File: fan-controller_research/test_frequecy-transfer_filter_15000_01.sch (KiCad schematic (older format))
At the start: 25 parts, among them U401 TL071

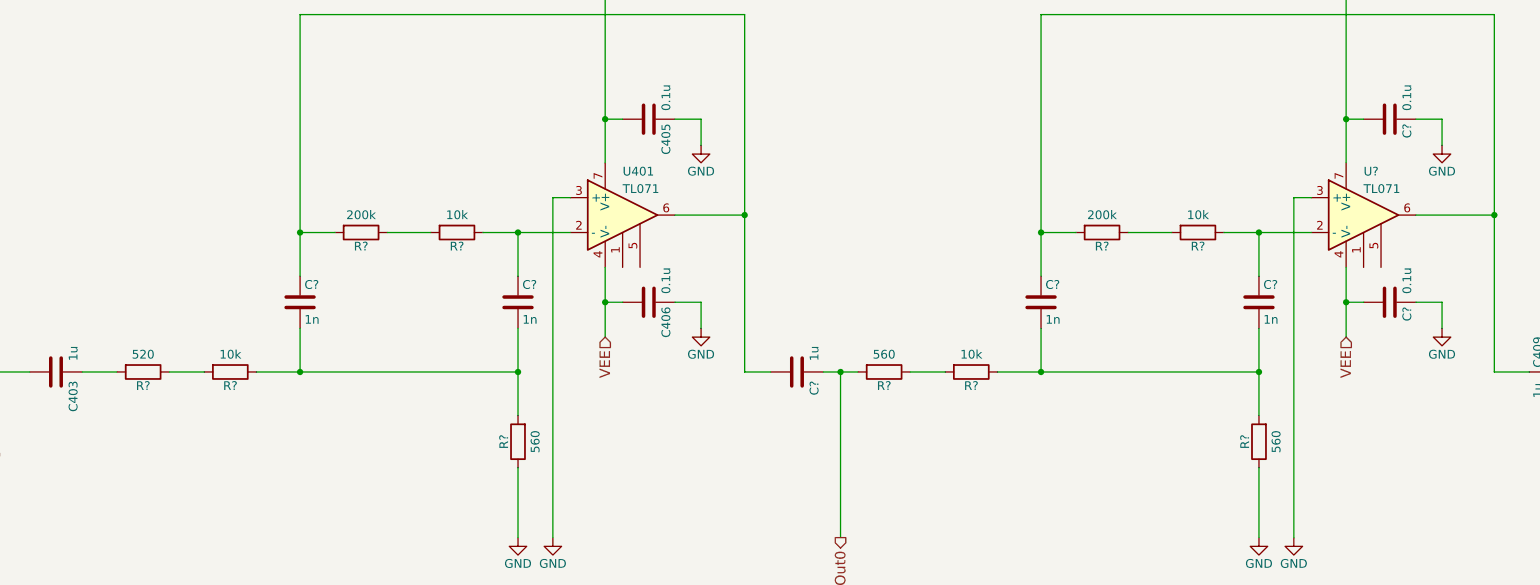
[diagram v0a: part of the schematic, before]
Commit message: Annotating schematics: 15000 Hz research filter
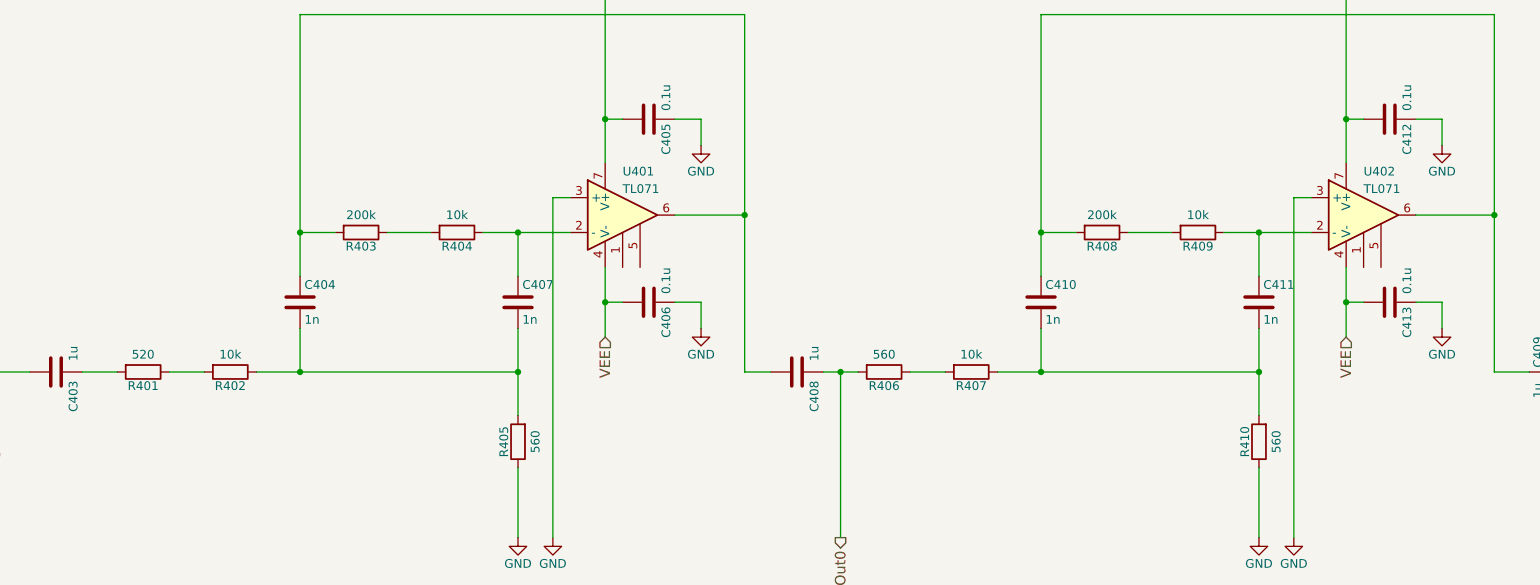
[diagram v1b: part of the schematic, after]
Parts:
- gave numbers to parts that had none: 18
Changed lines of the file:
@@
 $EndComp
 $Comp
-L AC #PWR013
+L AC #PWR404
 U 1 1 59072200
 P 3550 5100
-F 0 "#PWR013" H 3550 5000 50  0001 C CNN
+F 0 "#PWR404" H 3550 5000 50  0001 C CNN
 F 1 "AC" V 3300 5250 50  0000 C CNN
 F 2 "" H 3550 5100 50  0001 C CNN
@@
 $EndComp
 $Comp
-L GND #PWR014
+L GND #PWR405
 U 1 1 59072206
 P 3550 5450
-F 0 "#PWR014" H 3550 5200 50  0001 C CNN
+F 0 "#PWR405" H 3550 5200 50  0001 C CNN
 F 1 "GND" H 3550 5300 50  0000 C CNN
 F 2 "" H 3550 5450 50  0001 C CNN
@@
 $EndComp
 $Comp
-L GND #PWR015
+L GND #PWR411
 U 1 1 5907220C
 P 11050 5450
-F 0 "#PWR015" H 11050 5200 50  0001 C CNN
+F 0 "#PWR411" H 11050 5200 50  0001 C CNN
 F 1 "GND" H 11050 5300 50  0000 C CNN
 F 2 "" H 11050 5450 50  0001 C CNN
@@
 Spectrum analyzer output, 0 Hz ... 50 kHz.\n\nMarker is at 15 kHz.
 $Comp
-L +15V #PWR016
+L +15V #PWR401
 U 1 1 5907222C
 P 1000 850
-F 0 "#PWR016" H 1000 700 50  0001 C CNN
+F 0 "#PWR401" H 1000 700 50  0001 C CNN
 F 1 "+15V" H 1000 990 50  0000 C CNN
 F 2 "" H 1000 850 50  0001 C CNN
@@
 $EndComp
 $Comp
-L -15V #PWR404
+L -15V #PWR402
 U 1 1 59072240
 P 1000 2100
-F 0 "#PWR404" H 1000 2200 50  0001 C CNN
+F 0 "#PWR402" H 1000 2200 50  0001 C CNN
 F 1 "-15V" H 1000 2250 50  0000 C CNN
 F 2 "" H 1000 2100 50  0001 C CNN
@@
 VEE
 $Comp
-L GND #PWR017
+L GND #PWR403
 U 1 1 59072248
 P 1500 1550
-F 0 "#PWR017" H 1500 1300 50  0001 C CNN
+F 0 "#PWR403" H 1500 1300 50  0001 C CNN
 F 1 "GND" H 1500 1400 50  0000 C CNN
 F 2 "" H 1500 1550 50  0001 C CNN
@@
 $EndComp
 $Comp
-L GND #PWR018
+L GND #PWR408
 U 1 1 5907226B
 P 7650 3200
-F 0 "#PWR018" H 7650 2950 50  0001 C CNN
+F 0 "#PWR408" H 7650 2950 50  0001 C CNN
 F 1 "GND" H 7650 3050 50  0000 C CNN
 F 2 "" H 7650 3200 50  0001 C CNN
@@
 $EndComp
 $Comp
-L GND #PWR019
+L GND #PWR409
 U 1 1 59072271
 P 7650 4250
-F 0 "#PWR019" H 7650 4000 50  0001 C CNN
+F 0 "#PWR409" H 7650 4000 50  0001 C CNN
 F 1 "GND" H 7650 4100 50  0000 C CNN
 F 2 "" H 7650 4250 50  0001 C CNN
@@
 Two times cascaded: \n15 kHz band pass, using a \nmodified Deliyannis filter\n(Texas Instruments, SLOA093)
 $Comp
-L R R?
+L R R401
 U 1 1 590DFFD6
 P 4450 4500
-F 0 "R?" V 4530 4500 50  0000 C CNN
+F 0 "R401" V 4530 4500 50  0000 C CNN
 F 1 "520" V 4350 4500 50  0000 C CNN
 F 2 "" V 4380 4500 50  0001 C CNN
@@
 $EndComp
 $Comp
-L R R?
+L R R402
 U 1 1 590E0205
 P 4950 4500
-F 0 "R?" V 5030 4500 50  0000 C CNN
+F 0 "R402" V 5030 4500 50  0000 C CNN
 F 1 "10k" V 4850 4500 50  0000 C CNN
 F 2 "" V 4880 4500 50  0001 C CNN
@@
 $EndComp
 $Comp
-L C C?
+L C C404
 U 1 1 590E0538
 P 5350 4100
-F 0 "C?" H 5375 4200 50  0000 L CNN
+F 0 "C404" H 5375 4200 50  0000 L CNN
 F 1 "1n" H 5375 4000 50  0000 L CNN
 F 2 "" H 5388 3950 50  0001 C CNN
@@
 $EndComp
 $Comp
-L C C?
+L C C407
 U 1 1 590E08E5
 P 6600 4100
-F 0 "C?" H 6625 4200 50  0000 L CNN
+F 0 "C407" H 6625 4200 50  0000 L CNN
 F 1 "1n" H 6625 4000 50  0000 L CNN
 F 2 "" H 6638 3950 50  0001 C CNN
@@
 $EndComp
 $Comp
-L R R?
+L R R403
 U 1 1 590E0977
 P 5700 3700
-F 0 "R?" V 5780 3700 50  0000 C CNN
+F 0 "R403" V 5780 3700 50  0000 C CNN
 F 1 "200k" V 5600 3700 50  0000 C CNN
 F 2 "" V 5630 3700 50  0001 C CNN
@@
 $EndComp
 $Comp
-L R R?
+L R R404
 U 1 1 590E0A08
 P 6250 3700
-F 0 "R?" V 6330 3700 50  0000 C CNN
+F 0 "R404" V 6330 3700 50  0000 C CNN
 F 1 "10k" V 6150 3700 50  0000 C CNN
 F 2 "" V 6180 3700 50  0001 C CNN
@@
 $EndComp
 $Comp
-L R R?
+L R R405
 U 1 1 590E1314
 P 6600 4900
-F 0 "R?" V 6680 4900 50  0000 C CNN
+F 0 "R405" V 6680 4900 50  0000 C CNN
 F 1 "560" V 6500 4900 50  0000 C CNN
 F 2 "" V 6530 4900 50  0001 C CNN
@@
 $EndComp
 $Comp
-L GND #PWR?
+L GND #PWR406
 U 1 1 590E1431
 P 6600 5450
-F 0 "#PWR?" H 6600 5200 50  0001 C CNN
+F 0 "#PWR406" H 6600 5200 50  0001 C CNN
 F 1 "GND" H 6600 5300 50  0000 C CNN
 F 2 "" H 6600 5450 50  0001 C CNN
@@
 $EndComp
 $Comp
-L TL071 U?
+L TL071 U402
 U 1 1 590E2308
 P 11450 3600
-F 0 "U?" H 11450 3850 50  0000 L CNN
+F 0 "U402" H 11450 3850 50  0000 L CNN
 F 1 "TL071" H 11450 3750 50  0000 L CNN
 F 2 "" H 11500 3650 50  0001 C CNN
@@
 $EndComp
 $Comp
-L C C?
+L C C408
 U 1 1 590E230E
 P 8200 4500
-F 0 "C?" H 8250 4600 50  0000 L CNN
+F 0 "C408" H 8250 4600 50  0000 L CNN
 F 1 "1u" H 8050 4600 50  0000 L CNN
 F 2 "" H 8238 4350 50  0001 C CNN
@@
 $EndComp
 $Comp
-L GND #PWR?
+L GND #PWR412
 U 1 1 590E2318
 P 11900 3200
-F 0 "#PWR?" H 11900 2950 50  0001 C CNN
+F 0 "#PWR412" H 11900 2950 50  0001 C CNN
 F 1 "GND" H 11900 3050 50  0000 C CNN
 F 2 "" H 11900 3200 50  0001 C CNN
@@
 $EndComp
 $Comp
-L GND #PWR?
+L GND #PWR413
 U 1 1 590E231E
 P 11900 4250
-F 0 "#PWR?" H 11900 4000 50  0001 C CNN
+F 0 "#PWR413" H 11900 4000 50  0001 C CNN
 F 1 "GND" H 11900 4100 50  0000 C CNN
 F 2 "" H 11900 4250 50  0001 C CNN
@@
 $EndComp
 $Comp
-L C C?
+L C C412
 U 1 1 590E2324
 P 11600 3050
-F 0 "C?" H 11625 3150 50  0000 L CNN
+F 0 "C412" H 11625 3150 50  0000 L CNN
 F 1 "0.1u" H 11400 3150 50  0000 L CNN
 F 2 "" H 11638 2900 50  0001 C CNN
@@
 $EndComp
 $Comp
-L C C?
+L C C413
 U 1 1 590E232A
 P 11600 4100
-F 0 "C?" H 11625 4200 50  0000 L CNN
+F 0 "C413" H 11625 4200 50  0000 L CNN
 F 1 "0.1u" H 11400 4200 50  0000 L CNN
 F 2 "" H 11638 3950 50  0001 C CNN
@@
 VEE
 $Comp
-L R R?
+L R R406
 U 1 1 590E233A
 P 8700 4500
-F 0 "R?" V 8780 4500 50  0000 C CNN
+F 0 "R406" V 8780 4500 50  0000 C CNN
 F 1 "560" V 8600 4500 50  0000 C CNN
 F 2 "" V 8630 4500 50  0001 C CNN
@@
 $EndComp
 $Comp
-L R R?
+L R R407
 U 1 1 590E2340
 P 9200 4500
-F 0 "R?" V 9280 4500 50  0000 C CNN
+F 0 "R407" V 9280 4500 50  0000 C CNN
 F 1 "10k" V 9100 4500 50  0000 C CNN
 F 2 "" V 9130 4500 50  0001 C CNN
@@
 $EndComp
 $Comp
-L C C?
+L C C410
 U 1 1 590E2346
 P 9600 4100
-F 0 "C?" H 9625 4200 50  0000 L CNN
+F 0 "C410" H 9625 4200 50  0000 L CNN
 F 1 "1n" H 9625 4000 50  0000 L CNN
 F 2 "" H 9638 3950 50  0001 C CNN
@@
 $EndComp
 $Comp
-L C C?
+L C C411
 U 1 1 590E234C
 P 10850 4100
-F 0 "C?" H 10875 4200 50  0000 L CNN
+F 0 "C411" H 10875 4200 50  0000 L CNN
 F 1 "1n" H 10875 4000 50  0000 L CNN
 F 2 "" H 10888 3950 50  0001 C CNN
@@
 $EndComp
 $Comp
-L R R?
+L R R408
 U 1 1 590E2352
 P 9950 3700
-F 0 "R?" V 10030 3700 50  0000 C CNN
+F 0 "R408" V 10030 3700 50  0000 C CNN
 F 1 "200k" V 9850 3700 50  0000 C CNN
 F 2 "" V 9880 3700 50  0001 C CNN
@@
 $EndComp
 $Comp
-L R R?
+L R R409
 U 1 1 590E2358
 P 10500 3700
-F 0 "R?" V 10580 3700 50  0000 C CNN
+F 0 "R409" V 10580 3700 50  0000 C CNN
 F 1 "10k" V 10400 3700 50  0000 C CNN
 F 2 "" V 10430 3700 50  0001 C CNN
@@
 $EndComp
 $Comp
-L R R?
+L R R410
 U 1 1 590E236B
 P 10850 4900
-F 0 "R?" V 10930 4900 50  0000 C CNN
+F 0 "R410" V 10930 4900 50  0000 C CNN
 F 1 "560" V 10750 4900 50  0000 C CNN
 F 2 "" V 10780 4900 50  0001 C CNN
@@
 $EndComp
 $Comp
-L GND #PWR?
+L GND #PWR410
 U 1 1 590E2372
 P 10850 5450
-F 0 "#PWR?" H 10850 5200 50  0001 C CNN
+F 0 "#PWR410" H 10850 5200 50  0001 C CNN
 F 1 "GND" H 10850 5300 50  0000 C CNN
 F 2 "" H 10850 5450 50  0001 C CNN
@@
 $EndComp
 $Comp
-L GND #PWR?
+L GND #PWR407
 U 1 1 590E2E58
 P 6800 5450
-F 0 "#PWR?" H 6800 5200 50  0001 C CNN
+F 0 "#PWR407" H 6800 5200 50  0001 C CNN
 F 1 "GND" H 6800 5300 50  0000 C CNN
 F 2 "" H 6800 5450 50  0001 C CNN
@@
 Data
 89 50 4E 47 0D 0A 1A 0A 00 00 00 0D 49 48 44 52 00 00 04 00 00 00 03 11 08 02 00 00 00 FD 52 53
-64 00 00 00 03 73 42 49 54 08 08 08 DB E1 4F E0 00 00 00 09 70 48 59 73 00 00 0E C3 00 00 0E C3
-01 C7 6F A8 64 00 00 20 00 49 44 41 54 78 9C EC BD 5B 97 24 B9 8D 26 F8 7D A0 79 44 56 49 EA 6E
+64 00 00 00 03 73 42 49 54 08 08 08 DB E1 4F E0 00 00 00 09 70 48 59 73 00 00 0E 74 00 00 0E 74
+01 6B 24 B3 D6 00 00 20 00 49 44 41 54 78 9C EC BD 5B 97 24 B9 8D 26 F8 7D A0 79 44 56 49 EA 6E
 75 CF EE 9C D9 DB FF FF 3F FB BA EF 7B 99 3E A3 19 75 49 55 19 E1 04 F6 01 24 0C 24 CD 3C 3C 22
 23 2B B3 4A 01 A5 BC 3C CC 69 24 08 82 20 00 82 20 7F FC F1 47 00 00 CC 2C 3E 01 A8 2A 8E A0 50
@@
 Data
 89 50 4E 47 0D 0A 1A 0A 00 00 00 0D 49 48 44 52 00 00 04 00 00 00 03 09 08 02 00 00 00 12 D7 D3
-92 00 00 00 03 73 42 49 54 08 08 08 DB E1 4F E0 00 00 00 09 70 48 59 73 00 00 0E C3 00 00 0E C3
-01 C7 6F A8 64 00 00 20 00 49 44 41 54 78 9C AC BD DB 8E 2C B9 92 25 B6 8C F4 C8 DC 75 CE B4 A0
+92 00 00 00 03 73 42 49 54 08 08 08 DB E1 4F E0 00 00 00 09 70 48 59 73 00 00 0E 74 00 00 0E 74
+01 6B 24 B3 D6 00 00 20 00 49 44 41 54 78 9C AC BD DB 8E 2C B9 92 25 B6 8C F4 C8 DC 75 CE B4 A0
 3F 11 04 68 20 0C 24 41 D0 83 A0 FF FF 93 C1 F4 F4 A9 9D 19 4E 33 3D 98 73 C5 A2 D1 23 4F 75 4B
 AC 8D 28 4F 77 3A 69 77 9A 19 2F 6E FF D7 FF FA 9F CD AC B5 66 66 66 06 20 66 E9 BD B7 D6 22 62

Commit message: Communication system
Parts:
- renumbered C405 to C403, C412 to C404, C404 to C405, C407 to C406, C406 to C407, C410 to C408, C411 to C409, C413 to C410, C403 to C411, C408 to C412, C409 to C413, R403 to R401, R404 to R402, R408 to R403, R409 to R404, R401 to R405, R402 to R406, R406 to R407, R407 to R408, R405 to R409
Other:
- note added: "Components used do vary, so \nin this experiment the filter is not \nat it's best performance.\nPeak is at 14.4 kHz, -6dB points \nare at 13.2 kHz and 15.8 kHz.\nTotal bandwidth is 2.6 kHz. \n\nThis result is satisfactory as we\ncan expect better performance \nwhen we use better components.\n"
- note added: "Final values for resistors"
- note added: "R1: 10610\n->\n10k\n604\n6.04"
- note added: "R2: 558\n->\n549\n9.09"
- note added: "R3+R4: 212206\n->\n210k\n2.21k"
- note added: "Source data for\na single stage filter."
- note added: "Two times cascaded: \n15 kHz band pass, using a \nmodified Deliyannis filter\n(Texas Instruments, SLOA093)\n\nAll resistors: E96 series\nAll capacitors: E24 series"
- note removed: "Components used do vary, so \nin this experiment the filter is not \nat it's best performance.\nPeak is at 14.4 kHz, -6dB points \nare at 13.2 kHz and 15.8 kHz.\nTotal bandwidth is 2.6 kHz. \n\nThis result is satisfactory as we\ncan expect better performance \nwhen we use better components.\n\nAlso, there's room for optimization \nwith the resistors-in-series combinations."
- note removed: "Two times cascaded: \n15 kHz band pass, using a \nmodified Deliyannis filter\n(Texas Instruments, SLOA093)"
- moved on the sheet: C403, C404, C405, C406, C407, C408, C409, C410, C411, C412, C413, R401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
